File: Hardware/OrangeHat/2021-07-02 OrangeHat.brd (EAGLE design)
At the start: 84.8 x 55.9 mm, 28 parts, among them CON485A JACK_SMD_3MM5, CON485B JACK_SMD_3MM5, IC485 SN75176

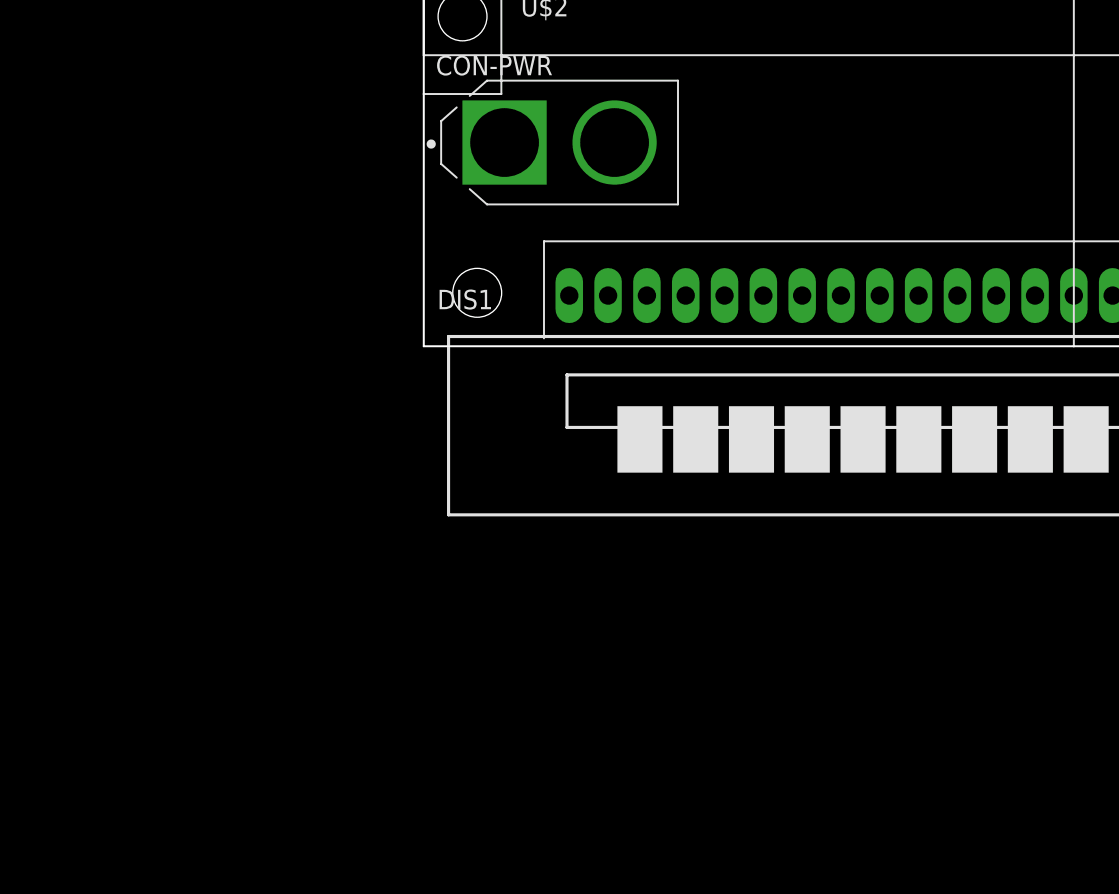
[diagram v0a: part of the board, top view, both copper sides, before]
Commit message: Add files via upload
LCD Display Schematics and Initial Placement
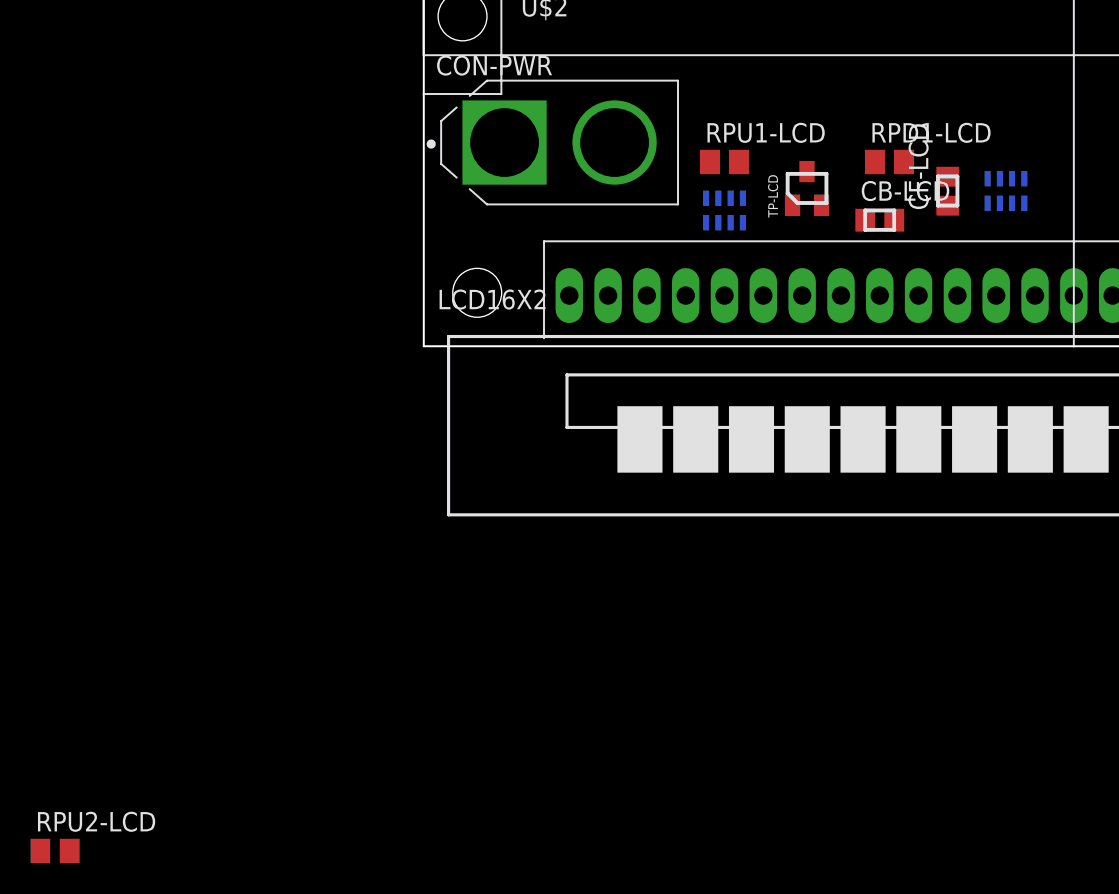
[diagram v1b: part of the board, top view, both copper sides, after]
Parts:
- added CB-LCD: 100n 50V, 2021-07-02 OrangeHat Library:C0805
- added CF-LCD: 10n, 2021-07-02 OrangeHat Library:C0805
- added RPD1-LCD: 1k, 2021-07-02 OrangeHat Library:M0805
- added RPU1-LCD, RPU2-LCD: 8.2k, 2021-07-02 OrangeHat Library:M0805
- added RS1-LCD, RS2-LCD: 4X 1K, 2021-07-02 OrangeHat Library:RAC1206
- added TP-LCD: MOS-P-SOT23, 2021-07-02 OrangeHat Library:SOT23
- renumbered DIS1 to LCD16X2
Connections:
- removed net N$14: LCD16X2.15
- removed net N$15: LCD16X2.16
- removed net N$3: LCD16X2.1
- removed net N$5: LCD16X2.2
- removed net N$6: LCD16X2.3
- removed net N$8: LCD16X2.5
- new net LCD-PMOS-G: RPU2-LCD.2, RS1-LCD.1B, TP-LCD.1
- new net UC-LCD-D4: RS2-LCD.1A
- new net UC-LCD-D5: RS2-LCD.2A
- new net UC-LCD-D6: RS2-LCD.3A
- new net UC-LCD-D7: RS2-LCD.4A
- new net UC-LCD-EN: RS1-LCD.4A
- new net UC-LCD-PWR#: RS1-LCD.1A
- new net UC-LCD-RS: RS1-LCD.2A
- new net VLCD#: CF-LCD.2, LCD16X2.3, RPD1-LCD.2, RPU1-LCD.1
- new net VLCD+: CB-LCD.2, LCD16X2.15, LCD16X2.2, RPU1-LCD.2, TP-LCD.3
- net N$10: now also RS2-LCD.1B
- net N$11: now also RS2-LCD.2B
- net N$12: now also RS2-LCD.3B
- net N$13: now also RS2-LCD.4B
- net N$7: now also RS1-LCD.2B
- net N$9: now also RS1-LCD.4B
- net VUC+: now also RPU2-LCD.1, TP-LCD.2
- net VUC-: now also CB-LCD.1, CF-LCD.1, LCD16X2.1, LCD16X2.10, LCD16X2.16, LCD16X2.5, LCD16X2.7, LCD16X2.8, LCD16X2.9, RPD1-LCD.1
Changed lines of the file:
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@@
 </autorouter>
 <elements>
-<element name="DIS1" library="2021-07-02 OrangeHat Library" package="DISPLAY_16X2_90DEG" value="DISPLAY_16X2_90DEG" x="1.52" y="-10.91"/>
+<element name="LCD16X2" library="2021-07-02 OrangeHat Library" package="DISPLAY_16X2_90DEG" value="DISPLAY_16X2_90DEG" x="1.52" y="-10.91"/>
 <element name="CON-PWR" library="2021-07-02 OrangeHat Library" package="AMASS_XT60-M" value="XT60-M" x="8.89" y="13.335">
 <attribute name="AVAILABILITY" value="Unavailable" x="8.89" y="13.335" size="1.778" layer="27" display="off"/>
@@
 <element name="RPU485" library="2021-07-02 OrangeHat Library" package="M0805" value="720" x="64.135" y="14.605" rot="MR90"/>
 <element name="RPD485" library="2021-07-02 OrangeHat Library" package="M0805" value="720" x="64.135" y="9.525" rot="MR90"/>
+<element name="TP-LCD" library="2021-07-02 OrangeHat Library" package="SOT23" value="MOS-P-SOT23" x="25.085" y="10.33"/>
+<element name="CB-LCD" library="2021-07-02 OrangeHat Library" package="C0805" value="100n 50V" x="29.845" y="8.255"/>
+<element name="RS2-LCD" library="2021-07-02 OrangeHat Library" package="RAC1206" value="4X 1K" x="38.1" y="10.16" rot="MR180"/>
+<element name="RS1-LCD" library="2021-07-02 OrangeHat Library" package="RAC1206" value="4X 1K" x="19.685" y="8.89" rot="MR180"/>
+<element name="RPU1-LCD" library="2021-07-02 OrangeHat Library" package="M0805" value="8.2k" x="19.685" y="12.065"/>
+<element name="RPD1-LCD" library="2021-07-02 OrangeHat Library" package="M0805" value="1k" x="30.48" y="12.065"/>
+<element name="CF-LCD" library="2021-07-02 OrangeHat Library" package="C0805" value="10n" x="34.29" y="10.16" rot="R90"/>
+<element name="RPU2-LCD" library="2021-07-02 OrangeHat Library" package="M0805" value="8.2k" x="-24.13" y="-33.02"/>
 </elements>
 <signals>
@@
 <signal name="VUC-">
 <contactref element="IMU1" pad="COM"/>
+<contactref element="LCD16X2" pad="1"/>
+<contactref element="LCD16X2" pad="8"/>
+<contactref element="LCD16X2" pad="9"/>
+<contactref element="LCD16X2" pad="10"/>
+<contactref element="LCD16X2" pad="7"/>
+<contactref element="LCD16X2" pad="16"/>
+<contactref element="CB-LCD" pad="1"/>
+<contactref element="RPD1-LCD" pad="1"/>
+<contactref element="CF-LCD" pad="1"/>
+<contactref element="LCD16X2" pad="5"/>
+<wire x1="27.305" y1="3.32" x2="25.7175" y2="52.13" width="0" layer="19" extent="1-1"/>
+<wire x1="29.845" y1="3.32" x2="27.305" y2="3.32" width="0" layer="19" extent="1-1"/>
+<wire x1="32.385" y1="3.32" x2="29.845" y2="3.32" width="0" layer="19" extent="1-1"/>
+<wire x1="24.765" y1="3.32" x2="27.305" y2="3.32" width="0" layer="19" extent="1-1"/>
+<wire x1="19.685" y1="3.32" x2="24.765" y2="3.32" width="0" layer="19" extent="1-1"/>
+<wire x1="9.525" y1="3.32" x2="19.685" y2="3.32" width="0" layer="19" extent="1-1"/>
+<wire x1="47.625" y1="3.32" x2="32.385" y2="3.32" width="0" layer="19" extent="1-1"/>
+<wire x1="28.895" y1="8.255" x2="9.525" y2="3.32" width="0" layer="19" extent="1-1"/>
+<wire x1="29.53" y1="12.065" x2="28.895" y2="8.255" width="0" layer="19" extent="1-1"/>
+<wire x1="34.29" y1="9.21" x2="29.53" y2="12.065" width="0" layer="19" extent="1-1"/>
 </signal>
 <signal name="VUC+">
 <contactref element="IMU1" pad="VCC"/>
+<contactref element="TP-LCD" pad="2"/>
+<contactref element="RPU2-LCD" pad="1"/>
+<wire x1="26.035" y1="9.23" x2="23.1775" y2="52.13" width="0" layer="19" extent="1-1"/>
+<wire x1="-25.08" y1="-33.02" x2="26.035" y2="9.23" width="0" layer="19" extent="1-1"/>
 </signal>
 <signal name="IMU-SDA">
@@
 <contactref element="UC1" pad="40"/>
 </signal>
-<signal name="N$3">
-<contactref element="DIS1" pad="1"/>
-</signal>
-<signal name="N$5">
-<contactref element="DIS1" pad="2"/>
-</signal>
-<signal name="N$6">
-<contactref element="DIS1" pad="3"/>
+<signal name="VLCD+">
+<contactref element="LCD16X2" pad="2"/>
+<contactref element="LCD16X2" pad="15"/>
+<contactref element="TP-LCD" pad="3"/>
+<contactref element="CB-LCD" pad="2"/>
+<contactref element="RPU1-LCD" pad="2"/>
+<wire x1="30.795" y1="8.255" x2="20.635" y2="12.065" width="0" layer="19" extent="1-1"/>
+<wire x1="25.085" y1="11.43" x2="20.635" y2="12.065" width="0" layer="19" extent="1-1"/>
+<wire x1="12.065" y1="3.32" x2="25.085" y2="11.43" width="0" layer="19" extent="1-1"/>
+<wire x1="45.085" y1="3.32" x2="12.065" y2="3.32" width="0" layer="19" extent="1-1"/>
+</signal>
+<signal name="VLCD#">
+<contactref element="LCD16X2" pad="3"/>
+<contactref element="CF-LCD" pad="2"/>
+<contactref element="RPU1-LCD" pad="1"/>
+<contactref element="RPD1-LCD" pad="2"/>
+<wire x1="31.43" y1="12.065" x2="34.29" y2="11.11" width="0" layer="19" extent="1-1"/>
+<wire x1="18.735" y1="12.065" x2="31.43" y2="12.065" width="0" layer="19" extent="1-1"/>
+<wire x1="14.605" y1="3.32" x2="18.735" y2="12.065" width="0" layer="19" extent="1-1"/>
 </signal>
 <signal name="N$7">
-<contactref element="DIS1" pad="4"/>
-</signal>
-<signal name="N$8">
-<contactref element="DIS1" pad="5"/>
+<contactref element="LCD16X2" pad="4"/>
+<contactref element="RS1-LCD" pad="2B"/>
+<wire x1="17.145" y1="3.32" x2="19.285" y2="8.09" width="0" layer="19" extent="1-1"/>
 </signal>
 <signal name="N$9">
-<contactref element="DIS1" pad="6"/>
+<contactref element="LCD16X2" pad="6"/>
+<contactref element="RS1-LCD" pad="4B"/>
+<wire x1="22.225" y1="3.32" x2="20.885" y2="8.09" width="0" layer="19" extent="1-1"/>
 </signal>
 <signal name="N$10">
-<contactref element="DIS1" pad="11"/>
+<contactref element="LCD16X2" pad="11"/>
+<contactref element="RS2-LCD" pad="1B"/>
+<wire x1="34.925" y1="3.32" x2="36.9" y2="9.36" width="0" layer="19" extent="1-1"/>
 </signal>
 <signal name="N$11">
-<contactref element="DIS1" pad="12"/>
+<contactref element="LCD16X2" pad="12"/>
+<contactref element="RS2-LCD" pad="2B"/>
+<wire x1="37.465" y1="3.32" x2="37.7" y2="9.36" width="0" layer="19" extent="1-1"/>
 </signal>
 <signal name="N$12">
-<contactref element="DIS1" pad="13"/>
+<contactref element="LCD16X2" pad="13"/>
+<contactref element="RS2-LCD" pad="3B"/>
+<wire x1="40.005" y1="3.32" x2="38.5" y2="9.36" width="0" layer="19" extent="1-1"/>
 </signal>
 <signal name="N$13">
-<contactref element="DIS1" pad="14"/>
-</signal>
-<signal name="N$14">
-<contactref element="DIS1" pad="15"/>
-</signal>
-<signal name="N$15">
-<contactref element="DIS1" pad="16"/>
+<contactref element="LCD16X2" pad="14"/>
+<contactref element="RS2-LCD" pad="4B"/>
+<wire x1="39.3" y1="9.36" x2="42.545" y2="3.32" width="0" layer="19" extent="1-1"/>
 </signal>
 <signal name="RPI-SDA">
@@
 <wire x1="60.325" y1="24.445" x2="61.28" y2="27.305" width="0" layer="19" extent="16-16"/>
 </signal>
+<signal name="UC-LCD-D4">
+<contactref element="RS2-LCD" pad="1A"/>
+</signal>
+<signal name="UC-LCD-D5">
+<contactref element="RS2-LCD" pad="2A"/>
+</signal>
+<signal name="UC-LCD-D6">
+<contactref element="RS2-LCD" pad="3A"/>
+</signal>
+<signal name="UC-LCD-D7">
+<contactref element="RS2-LCD" pad="4A"/>
+</signal>
+<signal name="UC-LCD-EN">
+<contactref element="RS1-LCD" pad="4A"/>
+</signal>
+<signal name="UC-LCD-RS">
+<contactref element="RS1-LCD" pad="2A"/>
+</signal>
+<signal name="UC-LCD-PWR#">
+<contactref element="RS1-LCD" pad="1A"/>
+</signal>
+<signal name="LCD-PMOS-G">
+<contactref element="RS1-LCD" pad="1B"/>
+<contactref element="TP-LCD" pad="1"/>
+<contactref element="RPU2-LCD" pad="2"/>
+<wire x1="18.485" y1="8.09" x2="-23.18" y2="-33.02" width="0" layer="19" extent="1-16"/>
+<wire x1="24.135" y1="9.23" x2="18.485" y2="8.09" width="0" layer="19" extent="1-16"/>
+</signal>
 </signals>

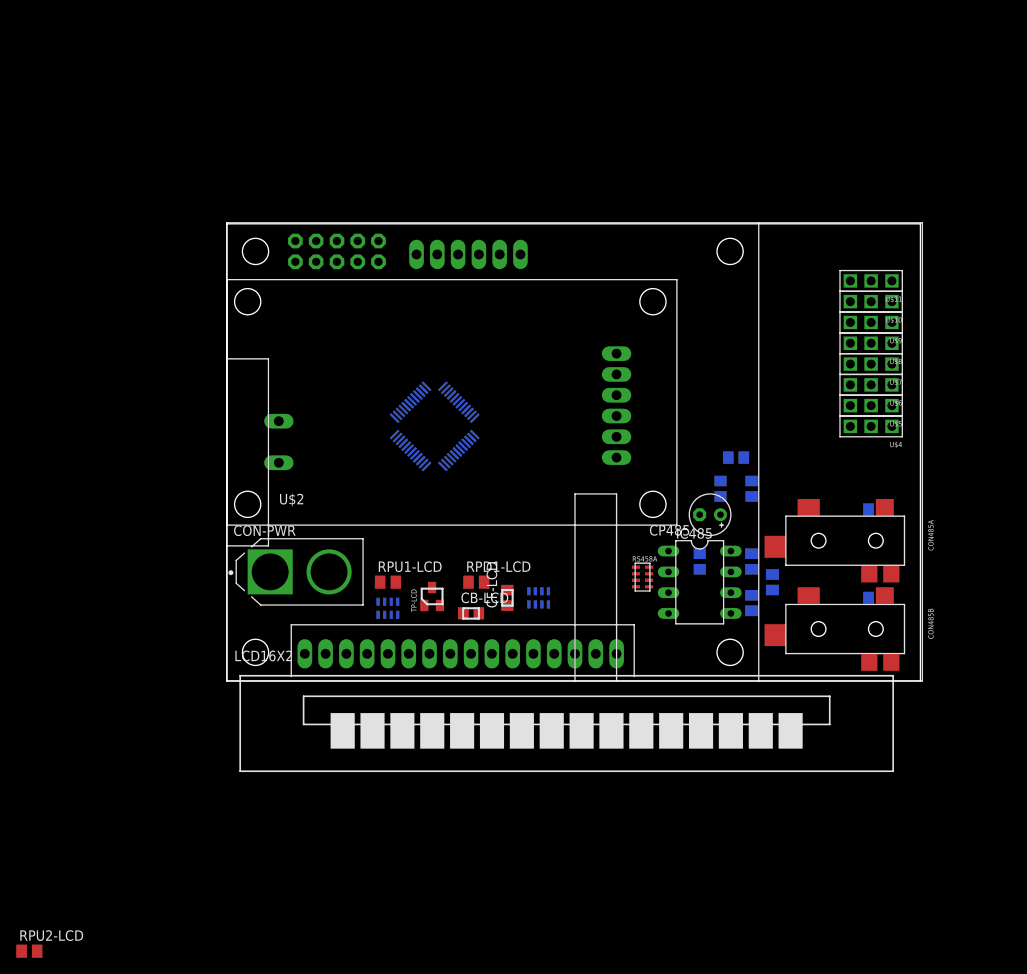
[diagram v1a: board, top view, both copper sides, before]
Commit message: Add files via upload
Added Servo schematics and initial placement. Adjusted/created footprints.
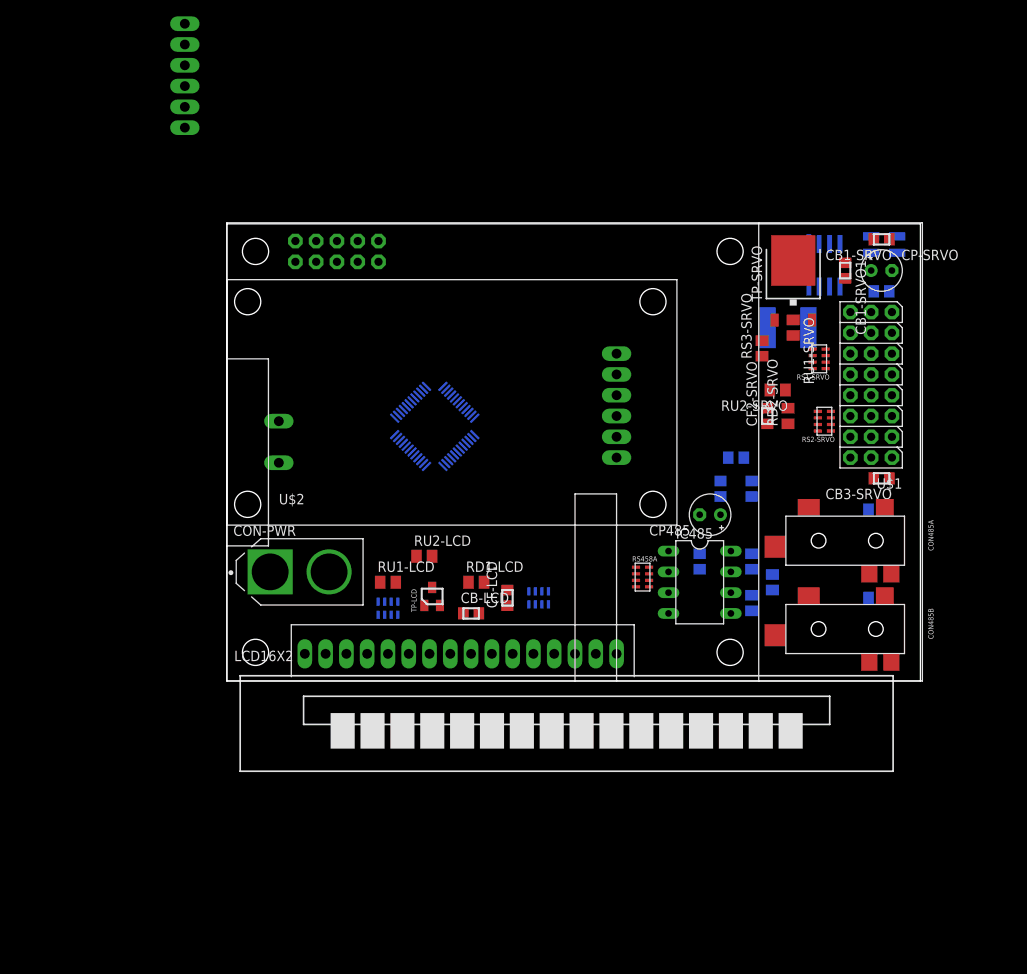
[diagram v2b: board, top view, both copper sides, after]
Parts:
- removed RPU2-LCD: 8.2k, 2021-07-02 OrangeHat Library:M0805
- removed U$10, U$11, U$4, U$5, U$6, U$7, U$8, U$9: PIWARSRPIHAT_CON3254-MIN, 2021-07-02 OrangeHat Library:PIWARSRPIHAT_CON3-254-MIN
- added CB1-SRVO, CB1-SRVO1, CB2-SRVO, CB3-SRVO: 1u, 2021-07-02 OrangeHat Library:C0805
- added CF2-SRVO: 10n, 2021-07-02 OrangeHat Library:C0805
- added CP-SRVO: 100uF 6V3, 2021-07-02 OrangeHat Library:E2,5-5
- added F-SRVO: PTC-M5040, 2021-07-02 OrangeHat Library:SMD-M5040
- added LF1-SRVO, LF1-SRVO1: BEAD 3A, 2021-07-02 OrangeHat Library:SMD-M2016
- added RD2-SRVO: 1k, 2021-07-02 OrangeHat Library:M0805
- added RS1-SRVO, RS2-SRVO: 4X 1K, 2021-07-02 OrangeHat Library:RAC1206
- added RS3-SRVO: 1K, 2021-07-02 OrangeHat Library:M0805
- added RU1-SRVO: 100k, 2021-07-02 OrangeHat Library:M0805
- added RU2-LCD, RU2-SRVO: 8.2k, 2021-07-02 OrangeHat Library:M0805
- added TP-SRVO: MOS-P-TO252, 2021-07-02 OrangeHat Library:TO252
- added U$1: SERVO8, 2021-07-02 OrangeHat Library:SERVO8
- added U$3: ACS712, 2021-07-02 OrangeHat Library:SO8
- moved IMU1 41.9 mm to (22.9, 66.0), turned to 0 degrees
- renumbered RPD1-LCD to RD1-LCD, RPU1-LCD to RU1-LCD
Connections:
- new net N$15: CB1-SRVO.1, LF1-SRVO1.1
- new net N$21: CB1-SRVO1.2, U$3.6
- new net N$23: RS2-SRVO.1A, U$1.8
- new net N$24: RS2-SRVO.2A, U$1.7
- new net N$25: RS2-SRVO.3A, U$1.6
- new net N$26: RS2-SRVO.4A, U$1.5
- new net N$27: RS1-SRVO.1A, U$1.4
- new net N$28: RS1-SRVO.2A, U$1.3
- new net N$29: RS1-SRVO.3A, U$1.2
- new net N$3: F-SRVO.1
- new net N$30: RS1-SRVO.4A, U$1.1
- new net N$5: RS3-SRVO.2, RU1-SRVO.2, TP-SRVO.1
- new net N$6: F-SRVO.2, RU1-SRVO.1, TP-SRVO.2
- new net UC-ISRVO: U$3.7
- new net UC-SRVO-PWR#: RS3-SRVO.1
- new net UC-SRVO1: RS1-SRVO.4B
- new net UC-SRVO2: RS1-SRVO.3B
- new net UC-SRVO3: RS1-SRVO.2B
- new net UC-SRVO4: RS1-SRVO.1B
- new net UC-SRVO5: RS2-SRVO.4B
- new net UC-SRVO6: RS2-SRVO.3B
- new net UC-SRVO7: RS2-SRVO.2B
- new net UC-SRVO8: RS2-SRVO.1B
- new net UC-VSRVO: CF2-SRVO.2, RD2-SRVO.2, RU2-SRVO.1
- new net VSRVO#A: RU2-SRVO.2, TP-SRVO.3, U$3.1, U$3.2
- new net VSRVO#B: CB1-SRVO.2, LF1-SRVO.1, U$3.3, U$3.4
- new net VSRVO+: CB2-SRVO.2, CB3-SRVO.2, CP-SRVO.+, LF1-SRVO.2, U$1.1+, U$1.2+, U$1.3+, U$1.4+, U$1.5+, U$1.6+, U$1.7+, U$1.8+
- new net VSRVO-: CB2-SRVO.1, CB3-SRVO.1, CP-SRVO.-, LF1-SRVO1.2, U$1.1-, U$1.2-, U$1.3-, U$1.4-, U$1.5-, U$1.6-, U$1.7-, U$1.8-
- net LCD-PMOS-G: now also RU2-LCD.2; no longer RPU2-LCD.2
- net VUC+: now also RU2-LCD.1, U$3.8; no longer RPU2-LCD.1
- net VUC-: now also CB1-SRVO1.1, CF2-SRVO.1, RD2-SRVO.1, U$3.5
